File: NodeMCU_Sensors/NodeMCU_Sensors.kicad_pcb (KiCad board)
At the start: 2 copper layers, 10 parts, among them J1 Conn_02x15_Odd_Even, J2 Conn_02x15_Odd_Even, J3 Conn_01x04, J4 Conn_01x04, J5 Conn_01x04, J6 Audio-Jack-3_2Switches, J7 Audio-Jack-3_2Switches, J8 Audio-Jack-3_2Switches, SW1 SW_Push

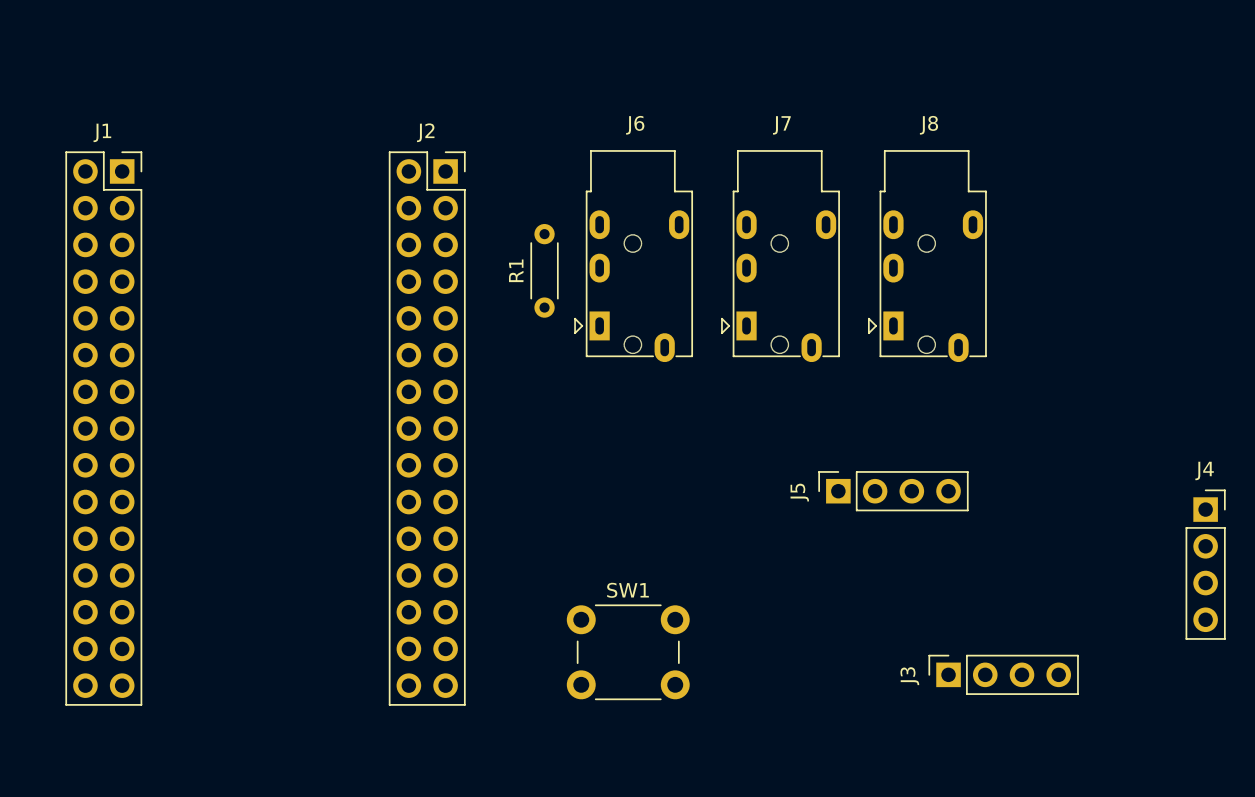
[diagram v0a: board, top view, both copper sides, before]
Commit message: Place parts according to layout plan
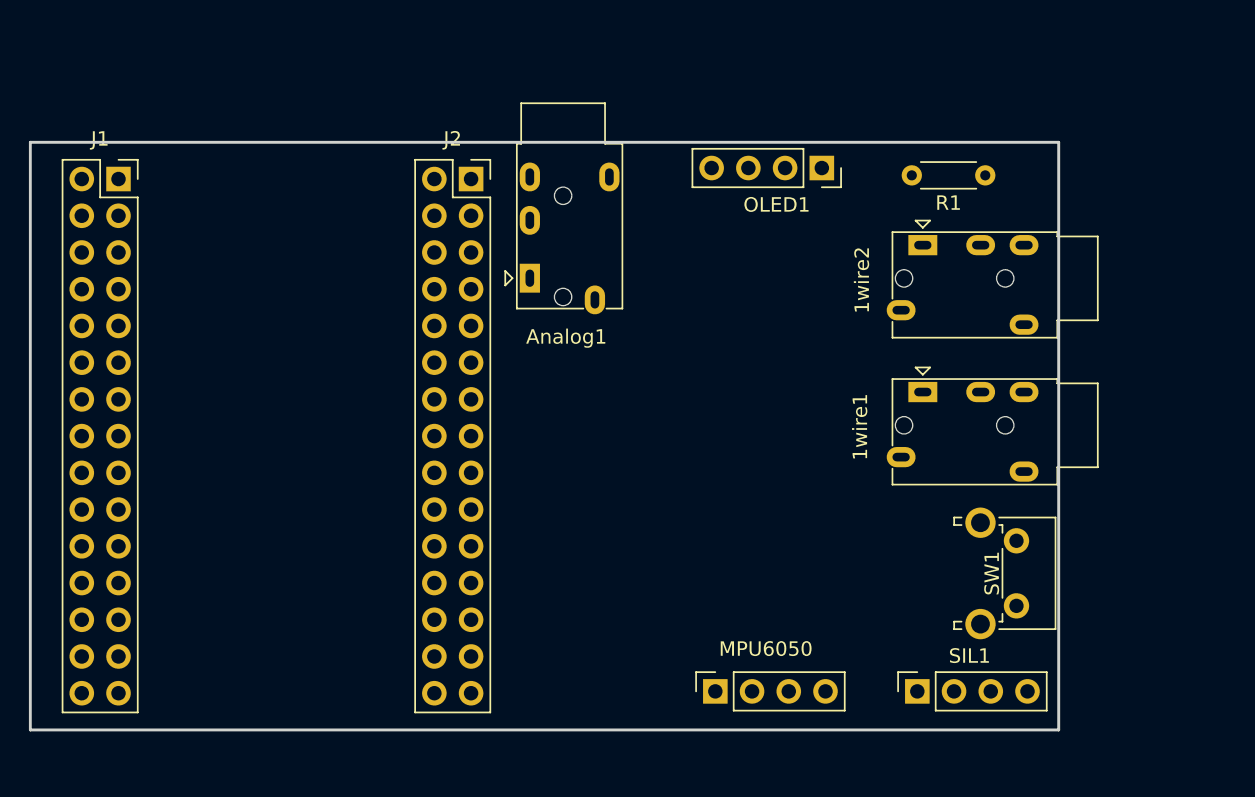
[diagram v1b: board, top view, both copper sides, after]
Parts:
- removed J3, J4, J5: Conn_01x04, Connector_PinSocket_2.54mm:PinSocket_1x04_P2.54mm_Vertical
- removed J6, J7, J8: Audio-Jack-3_2Switches, Connector_Audio:Jack_3.5mm_PJ320E_Horizontal
- added 1wire1: Audio-Jack-3_2Switches, Connector_Audio:Jack_3.5mm_PJ320E_Horizontal, F.Cu at (155.7, 80.8)
- added 1wire2: Audio-Jack-3_2Switches, Connector_Audio:Jack_3.5mm_PJ320E_Horizontal, F.Cu at (155.7, 70.6)
- added Analog1: Audio-Jack-3_2Switches, Connector_Audio:Jack_3.5mm_PJ320E_Horizontal, F.Cu at (128.5, 72.9)
- added MPU6050: Conn_01x04, Connector_PinSocket_2.54mm:PinSocket_1x04_P2.54mm_Vertical, F.Cu at (141.4, 101.5)
- added OLED1: Conn_01x04, Connector_PinSocket_2.54mm:PinSocket_1x04_P2.54mm_Vertical, F.Cu at (148.7, 65.3)
- added SIL1: Conn_01x04, Connector_PinSocket_2.54mm:PinSocket_1x04_P2.54mm_Vertical, F.Cu at (155.3, 101.5)
- SW1: footprint Button_Switch_THT:SW_PUSH_6mm -> Button_Switch_THT:SW_Tactile_SPST_Angled_PTS645Vx39-2LFS
- moved R1 31.8 mm to (160.0, 65.8), turned to 180 degrees
- moved SW1 30.6 mm to (162.2, 91.1), turned to 270 degrees
- moved J2 1.84 mm to (124.5, 66.0)
- moved J1 0.58 mm to (100.1, 66.0)
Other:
- board outline added: 71.1 x 40.6 mm

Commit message: Wire up i2c sensors
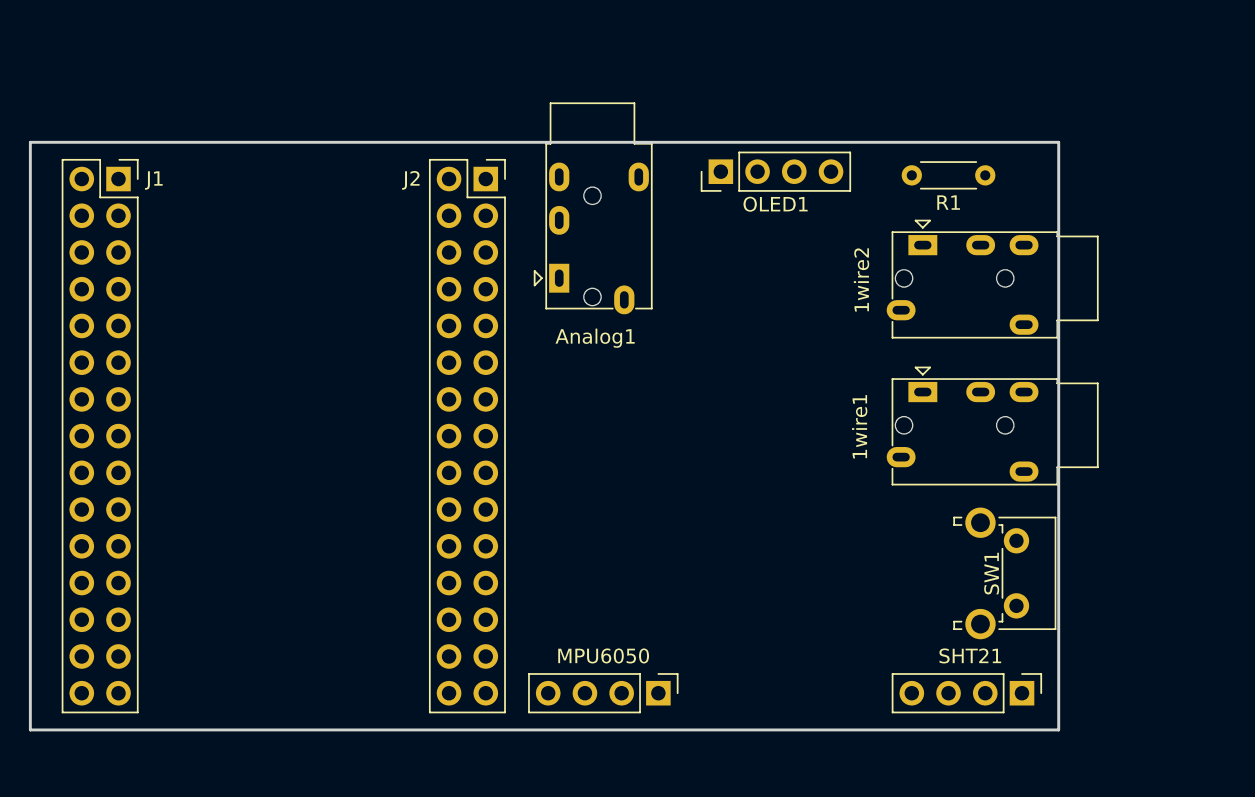
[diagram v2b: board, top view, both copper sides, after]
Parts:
- removed SIL1: Conn_01x04, Connector_PinSocket_2.54mm:PinSocket_1x04_P2.54mm_Vertical
- added SHT21: Conn_01x04, Socket_Strips:Socket_Strip_Straight_1x04_Pitch2.54mm, F.Cu at (162.6, 101.6)
- J1, J2: footprint Connector_PinSocket_2.54mm:PinSocket_2x15_P2.54mm_Vertical -> Socket_Strips:Socket_Strip_Straight_2x15_Pitch2.54mm
- MPU6050, OLED1: footprint Connector_PinSocket_2.54mm:PinSocket_1x04_P2.54mm_Vertical -> Socket_Strips:Socket_Strip_Straight_1x04_Pitch2.54mm
- moved OLED1 6.99 mm to (141.7, 65.5), turned to 90 degrees
- moved MPU6050 3.94 mm to (137.4, 101.6), turned to 270 degrees
- moved Analog1 2.03 mm to (130.6, 72.9)
- moved J2 1.02 mm to (125.5, 66.0)
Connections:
- MPU6050 pad 1: Net-(MPU6050-Pad1) -> D2
- MPU6050 pad 2: Net-(MPU6050-Pad2) -> D1
- MPU6050 pad 3: Net-(MPU6050-Pad3) -> GND
- MPU6050 pad 4: Net-(MPU6050-Pad4) -> 3V3
- OLED1 pad 1: Net-(OLED1-Pad1) -> 3V3
- OLED1 pad 2: Net-(OLED1-Pad2) -> GND
- OLED1 pad 3: Net-(OLED1-Pad3) -> D1
- OLED1 pad 4: Net-(OLED1-Pad4) -> D2

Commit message: Route 3.5mm jacks
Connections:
- 1wire1 pad 1: Net-(1wire1-Pad1) -> D7
- 1wire1 pad 2: Net-(1wire1-Pad2) -> D6
- 1wire1 pad 3: Net-(1wire1-Pad3) -> D8
- 1wire1 pad 4: Net-(1wire1-Pad4) -> (no net)
- 1wire1 pad 5: Net-(1wire1-Pad5) -> (no net)
- 1wire2 pad 1: Net-(1wire2-Pad1) -> D7
- 1wire2 pad 2: Net-(1wire2-Pad2) -> D6
- 1wire2 pad 3: Net-(1wire2-Pad3) -> D8
- 1wire2 pad 4: Net-(1wire2-Pad4) -> (no net)
- 1wire2 pad 5: Net-(1wire2-Pad5) -> (no net)
- Analog1 pad 1: Net-(Analog1-Pad1) -> A0
- Analog1 pad 3: Net-(Analog1-Pad3) -> GND
- Analog1 pad 4: Net-(Analog1-Pad4) -> (no net)
- Analog1 pad 5: Net-(Analog1-Pad5) -> (no net)
- SW1 pad 1: Net-(SW1-Pad1) -> GND
- SW1 pad 2: Net-(SW1-Pad2) -> D5
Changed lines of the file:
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@@
     (zones 0)
     (modules 10)
-    (nets 45)
+    (nets 29)
   )
   (page A4)
@@
   (net 24 D1)
   (net 25 D0)
-  (net 26 "Net-(SW1-Pad2)")
-  (net 27 "Net-(SW1-Pad1)")
-  (net 28 RSV1)
-  (net 29 RSV2)
-  (net 30 "Net-(1wire1-Pad5)")
-  (net 31 "Net-(1wire1-Pad4)")
-  (net 32 "Net-(1wire1-Pad1)")
-  (net 33 "Net-(1wire1-Pad2)")
-  (net 34 "Net-(1wire1-Pad3)")
-  (net 35 "Net-(1wire2-Pad3)")
-  (net 36 "Net-(1wire2-Pad2)")
-  (net 37 "Net-(1wire2-Pad1)")
-  (net 38 "Net-(1wire2-Pad4)")
-  (net 39 "Net-(1wire2-Pad5)")
-  (net 40 "Net-(Analog1-Pad5)")
-  (net 41 "Net-(Analog1-Pad4)")
-  (net 42 "Net-(Analog1-Pad1)")
-  (net 43 "Net-(Analog1-Pad2)")
-  (net 44 "Net-(Analog1-Pad3)")
+  (net 26 RSV1)
+  (net 27 RSV2)
+  (net 28 "Net-(Analog1-Pad2)")
   (net_class Default "This is the default net class."
     (clearance 0.2)
@@
     (add_net EN)
     (add_net GND)
-    (add_net "Net-(1wire1-Pad1)")
-    (add_net "Net-(1wire1-Pad2)")
-    (add_net "Net-(1wire1-Pad3)")
-    (add_net "Net-(1wire1-Pad4)")
-    (add_net "Net-(1wire1-Pad5)")
-    (add_net "Net-(1wire2-Pad1)")
-    (add_net "Net-(1wire2-Pad2)")
-    (add_net "Net-(1wire2-Pad3)")
-    (add_net "Net-(1wire2-Pad4)")
-    (add_net "Net-(1wire2-Pad5)")
-    (add_net "Net-(Analog1-Pad1)")
     (add_net "Net-(Analog1-Pad2)")
-    (add_net "Net-(Analog1-Pad3)")
-    (add_net "Net-(Analog1-Pad4)")
-    (add_net "Net-(Analog1-Pad5)")
     (add_net "Net-(R1-Pad1)")
     (add_net "Net-(R1-Pad2)")
-    (add_net "Net-(SW1-Pad1)")
-    (add_net "Net-(SW1-Pad2)")
     (add_net RST)
     (add_net RSV1)
@@
     (pad 1 thru_hole rect (at 0 0 270) (size 1.7 1.7) (drill 1) (layers *.Cu *.Mask)
       (net 23 D2))
-    (model ${KISYS3DMOD}/Socket_Strips.3dshapes/Socket_Strip_Straight_1x04_Pitch2.54mm.wrl
-      (offset (xyz 0 -3.809999942779541 0))
-      (scale (xyz 1 1 1))
-      (rotate (xyz 0 0 270))
+    (model ${KISYS3DMOD}/Connector_PinSocket_2.54mm.3dshapes/PinSocket_1x04_P2.54mm_Vertical.step
+      (at (xyz 0 0 0))
+      (scale (xyz 1 1 1))
+      (rotate (xyz 0 0 0))
     )
   )
@@
     (pad 4 thru_hole oval (at 0 7.62 90) (size 1.7 1.7) (drill 1) (layers *.Cu *.Mask)
       (net 23 D2))
-    (model ${KISYS3DMOD}/Socket_Strips.3dshapes/Socket_Strip_Straight_1x04_Pitch2.54mm.wrl
-      (offset (xyz 0 -3.809999942779541 0))
-      (scale (xyz 1 1 1))
-      (rotate (xyz 0 0 270))
+    (model ${KISYS3DMOD}/Connector_PinSocket_2.54mm.3dshapes/PinSocket_1x04_P2.54mm_Vertical.step
+      (at (xyz 0 0 0))
+      (scale (xyz 1 1 1))
+      (rotate (xyz 0 0 0))
     )
   )
@@
     (pad 1 thru_hole rect (at 0 0 270) (size 1.7 1.7) (drill 1) (layers *.Cu *.Mask)
       (net 23 D2))
-    (model ${KISYS3DMOD}/Socket_Strips.3dshapes/Socket_Strip_Straight_1x04_Pitch2.54mm.wrl
-      (offset (xyz 0 -3.809999942779541 0))
-      (scale (xyz 1 1 1))
-      (rotate (xyz 0 0 270))
+    (model ${KISYS3DMOD}/Connector_PinSocket_2.54mm.3dshapes/PinSocket_1x04_P2.54mm_Vertical.step
+      (at (xyz 0 0 0))
+      (scale (xyz 1 1 1))
+      (rotate (xyz 0 0 0))
     )
   )
@@
     (pad 30 thru_hole oval (at -2.54 35.56) (size 1.7 1.7) (drill 1) (layers *.Cu *.Mask)
       (net 11 3V3))
-    (model ${KISYS3DMOD}/Socket_Strips.3dshapes/Socket_Strip_Straight_2x15_Pitch2.54mm.wrl
-      (offset (xyz -1.269999980926514 -17.77999973297119 0))
-      (scale (xyz 1 1 1))
-      (rotate (xyz 0 0 270))
+    (model ${KISYS3DMOD}/Connector_PinSocket_2.54mm.3dshapes/PinSocket_2x15_P2.54mm_Vertical.step
+      (at (xyz 0 0 0))
+      (scale (xyz 1 1 1))
+      (rotate (xyz 0 0 0))
     )
   )
@@
       (net 4 EDS))
     (pad 6 thru_hole oval (at -2.54 5.08) (size 1.7 1.7) (drill 1) (layers *.Cu *.Mask)
-      (net 29 RSV2))
+      (net 27 RSV2))
     (pad 5 thru_hole oval (at 0 5.08) (size 1.7 1.7) (drill 1) (layers *.Cu *.Mask)
-      (net 29 RSV2))
+      (net 27 RSV2))
     (pad 4 thru_hole oval (at -2.54 2.54) (size 1.7 1.7) (drill 1) (layers *.Cu *.Mask)
-      (net 28 RSV1))
+      (net 26 RSV1))
     (pad 3 thru_hole oval (at 0 2.54) (size 1.7 1.7) (drill 1) (layers *.Cu *.Mask)
-      (net 28 RSV1))
+      (net 26 RSV1))
     (pad 2 thru_hole oval (at -2.54 0) (size 1.7 1.7) (drill 1) (layers *.Cu *.Mask)
       (net 3 A0))
     (pad 1 thru_hole rect (at 0 0) (size 1.7 1.7) (drill 1) (layers *.Cu *.Mask)
       (net 3 A0))
-    (model ${KISYS3DMOD}/Socket_Strips.3dshapes/Socket_Strip_Straight_2x15_Pitch2.54mm.wrl
-      (offset (xyz -1.269999980926514 -17.77999973297119 0))
-      (scale (xyz 1 1 1))
-      (rotate (xyz 0 0 270))
+    (model ${KISYS3DMOD}/Connector_PinSocket_2.54mm.3dshapes/PinSocket_2x15_P2.54mm_Vertical.step
+      (at (xyz 0 0 0))
+      (scale (xyz 1 1 1))
+      (rotate (xyz 0 0 0))
     )
   )
@@
     (pad "" thru_hole circle (at 5.76 2.49 270) (size 2.1 2.1) (drill 1.3) (layers *.Cu *.Mask))
     (pad 2 thru_hole circle (at 4.5 0 270) (size 1.75 1.75) (drill 0.99) (layers *.Cu *.Mask)
-      (net 26 "Net-(SW1-Pad2)"))
+      (net 20 D5))
     (pad 1 thru_hole circle (at 0 0 270) (size 1.75 1.75) (drill 0.99) (layers *.Cu *.Mask)
-      (net 27 "Net-(SW1-Pad1)"))
+      (net 10 GND))
     (pad "" thru_hole circle (at -1.25 2.49 270) (size 2.1 2.1) (drill 1.3) (layers *.Cu *.Mask))
     (model ${KISYS3DMOD}/Button_Switch_THT.3dshapes/SW_Tactile_SPST_Angled_PTS645Vx39-2LFS.wrl
@@
     (fp_line (start -1.3 -12.5) (end 6.8 -12.5) (layer F.CrtYd) (width 0.05))
     (fp_circle (center 0.9 0) (end 1.2 0.15) (layer F.Fab) (width 0.12))
-    (pad 5 thru_hole oval (at 5.5 -7 270) (size 2 1.4) (drill oval 1.2 0.6) (layers *.Cu *.Mask)
-      (net 40 "Net-(Analog1-Pad5)"))
-    (pad 4 thru_hole oval (at 4.5 1.5 270) (size 2 1.4) (drill oval 1.2 0.6) (layers *.Cu *.Mask)
-      (net 41 "Net-(Analog1-Pad4)"))
+    (pad 5 thru_hole oval (at 5.5 -7 270) (size 2 1.4) (drill oval 1.2 0.6) (layers *.Cu *.Mask))
+    (pad 4 thru_hole oval (at 4.5 1.5 270) (size 2 1.4) (drill oval 1.2 0.6) (layers *.Cu *.Mask))
     (pad 1 thru_hole rect (at 0 0 270) (size 2 1.4) (drill oval 1.2 0.6) (layers *.Cu *.Mask)
-      (net 42 "Net-(Analog1-Pad1)"))
+      (net 3 A0))
     (pad 2 thru_hole oval (at 0 -4 270) (size 2 1.4) (drill oval 1.2 0.6) (layers *.Cu *.Mask)
-      (net 43 "Net-(Analog1-Pad2)"))
+      (net 28 "Net-(Analog1-Pad2)"))
     (pad 3 thru_hole oval (at 0 -7 270) (size 2 1.4) (drill oval 1.2 0.6) (layers *.Cu *.Mask)
-      (net 44 "Net-(Analog1-Pad3)"))
+      (net 10 GND))
     (pad "" np_thru_hole circle (at 2.3 -5.7 270) (size 1.2 1.2) (drill 1.2) (layers *.Cu *.Mask))
     (pad "" np_thru_hole circle (at 2.3 1.3 270) (size 1.2 1.2) (drill 1.2) (layers *.Cu *.Mask))
@@
     (pad "" np_thru_hole circle (at 2.3 -5.7 180) (size 1.2 1.2) (drill 1.2) (layers *.Cu *.Mask))
     (pad 3 thru_hole oval (at 0 -7 180) (size 2 1.4) (drill oval 1.2 0.6) (layers *.Cu *.Mask)
-      (net 35 "Net-(1wire2-Pad3)"))
+      (net 17 D8))
     (pad 2 thru_hole oval (at 0 -4 180) (size 2 1.4) (drill oval 1.2 0.6) (layers *.Cu *.Mask)
-      (net 36 "Net-(1wire2-Pad2)"))
+      (net 19 D6))
     (pad 1 thru_hole rect (at 0 0 180) (size 2 1.4) (drill oval 1.2 0.6) (layers *.Cu *.Mask)
-      (net 37 "Net-(1wire2-Pad1)"))
-    (pad 4 thru_hole oval (at 4.5 1.5 180) (size 2 1.4) (drill oval 1.2 0.6) (layers *.Cu *.Mask)
-      (net 38 "Net-(1wire2-Pad4)"))
-    (pad 5 thru_hole oval (at 5.5 -7 180) (size 2 1.4) (drill oval 1.2 0.6) (layers *.Cu *.Mask)
-      (net 39 "Net-(1wire2-Pad5)"))
+      (net 18 D7))
+    (pad 4 thru_hole oval (at 4.5 1.5 180) (size 2 1.4) (drill oval 1.2 0.6) (layers *.Cu *.Mask))
+    (pad 5 thru_hole oval (at 5.5 -7 180) (size 2 1.4) (drill oval 1.2 0.6) (layers *.Cu *.Mask))
     (model "${KIPRJMOD}/3dmodels/TRS Jack.stp"
       (offset (xyz 3 3 5.5))
@@
     (fp_line (start -1.3 -12.5) (end 6.8 -12.5) (layer F.CrtYd) (width 0.05))
     (fp_circle (center 0.9 0) (end 1.2 0.15) (layer F.Fab) (width 0.12))
-    (pad 5 thru_hole oval (at 5.5 -7 180) (size 2 1.4) (drill oval 1.2 0.6) (layers *.Cu *.Mask)
-      (net 30 "Net-(1wire1-Pad5)"))
-    (pad 4 thru_hole oval (at 4.5 1.5 180) (size 2 1.4) (drill oval 1.2 0.6) (layers *.Cu *.Mask)
-      (net 31 "Net-(1wire1-Pad4)"))
+    (pad 5 thru_hole oval (at 5.5 -7 180) (size 2 1.4) (drill oval 1.2 0.6) (layers *.Cu *.Mask))
+    (pad 4 thru_hole oval (at 4.5 1.5 180) (size 2 1.4) (drill oval 1.2 0.6) (layers *.Cu *.Mask))
     (pad 1 thru_hole rect (at 0 0 180) (size 2 1.4) (drill oval 1.2 0.6) (layers *.Cu *.Mask)
-      (net 32 "Net-(1wire1-Pad1)"))
+      (net 18 D7))
     (pad 2 thru_hole oval (at 0 -4 180) (size 2 1.4) (drill oval 1.2 0.6) (layers *.Cu *.Mask)
-      (net 33 "Net-(1wire1-Pad2)"))
+      (net 19 D6))
     (pad 3 thru_hole oval (at 0 -7 180) (size 2 1.4) (drill oval 1.2 0.6) (layers *.Cu *.Mask)
-      (net 34 "Net-(1wire1-Pad3)"))
+      (net 17 D8))
     (pad "" np_thru_hole circle (at 2.3 -5.7 180) (size 1.2 1.2) (drill 1.2) (layers *.Cu *.Mask))
     (pad "" np_thru_hole circle (at 2.3 1.3 180) (size 1.2 1.2) (drill 1.2) (layers *.Cu *.Mask))

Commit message: Basic autorouted board
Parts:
- added R2: 39K, Resistors_THT:R_Axial_DIN0204_L3.6mm_D1.6mm_P5.08mm_Horizontal, F.Cu at (113.8, 65.3)
- added R3: 10K, Resistors_THT:R_Axial_DIN0204_L3.6mm_D1.6mm_P5.08mm_Horizontal, F.Cu at (109.5, 70.4)
- R1: value R -> 4.7K
- moved 1wire1 2.80 mm to (155.8, 78.0)
- moved SW1 2.67 mm to (162.3, 88.4)
- moved 1wire2 2.03 mm to (155.7, 68.6)
- moved R1 0.51 mm to (160.0, 65.3)
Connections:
- 1wire1 pad 3: D8 -> GND
- 1wire2 pad 3: D8 -> GND
- Analog1 pad 1: A0 -> Net-(Analog1-Pad1)
- R1 pad 1: Net-(R1-Pad1) -> D6
- R1 pad 2: Net-(R1-Pad2) -> D7
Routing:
- net GND: track 0.00 -> 178.3 mm
- net 3V3: track 0.00 -> 107.4 mm
- net D2: track 0.00 -> 99.5 mm
- net D1: track 0.00 -> 94.3 mm
- net D6: track 0.00 -> 53.8 mm
- net D5: track 0.00 -> 52.4 mm
- net D7: track 0.00 -> 50.8 mm
- net Net-(Analog1-Pad1): track 0.00 -> 17.8 mm
- net A0: track 0.00 -> 16.6 mm
- net VIN: track 0.00 -> 2.54 mm
- net TX: track 0.00 -> 2.54 mm
- net SD2: track 0.00 -> 2.54 mm
- net SD1: track 0.00 -> 2.54 mm
- net SD0: track 0.00 -> 2.54 mm
- net RX: track 0.00 -> 2.54 mm
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- added copper zone on B.Cu, net GND
- added copper zone on F.Cu, net GND
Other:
- outline, holes or cut-outs redrawn
- net class Power added: clearance 0.5, trace_width 0.5, via_dia 0.8, via_drill 0.4
- board text added: "3V3"
- board text added: "A0"
- board text added: "CLK"
- board text added: "CMD"
- board text added: "D0"
- board text added: "D1"
- board text added: "D2"
- board text added: "D3"
- board text added: "D4"
- board text added: "D5"
- board text added: "D6"
- board text added: "D7"
- board text added: "D8"
- board text added: "EDS"
- board text added: "EN"
- board text added: "GND"
- board text added: "RST"
- board text added: "RSV1"
- board text added: "RSV2"
- board text added: "RX"
- board text added: "SCL"
- board text added: "SD0"
- board text added: "SD1"
- board text added: "SD2"
- board text added: "SDA"
- board text added: "TX"
- board text added: "VIN"

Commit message: Add version and project name
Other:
- board text added: "NodeMCU Sensor Node Whatnick INC v0.1 28/01/2018"
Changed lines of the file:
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@@
   (general
     (thickness 1.6)
-    (drawings 76)
+    (drawings 77)
     (tracks 158)
     (zones 0)
@@
     )
   )
+  (gr_text "NodeMCU Sensor Node\nWhatnick INC\nv0.1 28/01/2018" (at 144.272 84.836 90) (layer B.SilkS)
+    (effects (font (size 1.5 1.5) (thickness 0.3)) (justify mirror))
+  )
   (dimension 40.64 (width 0.3) (layer F.Fab)
